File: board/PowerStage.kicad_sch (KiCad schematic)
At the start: 36 parts

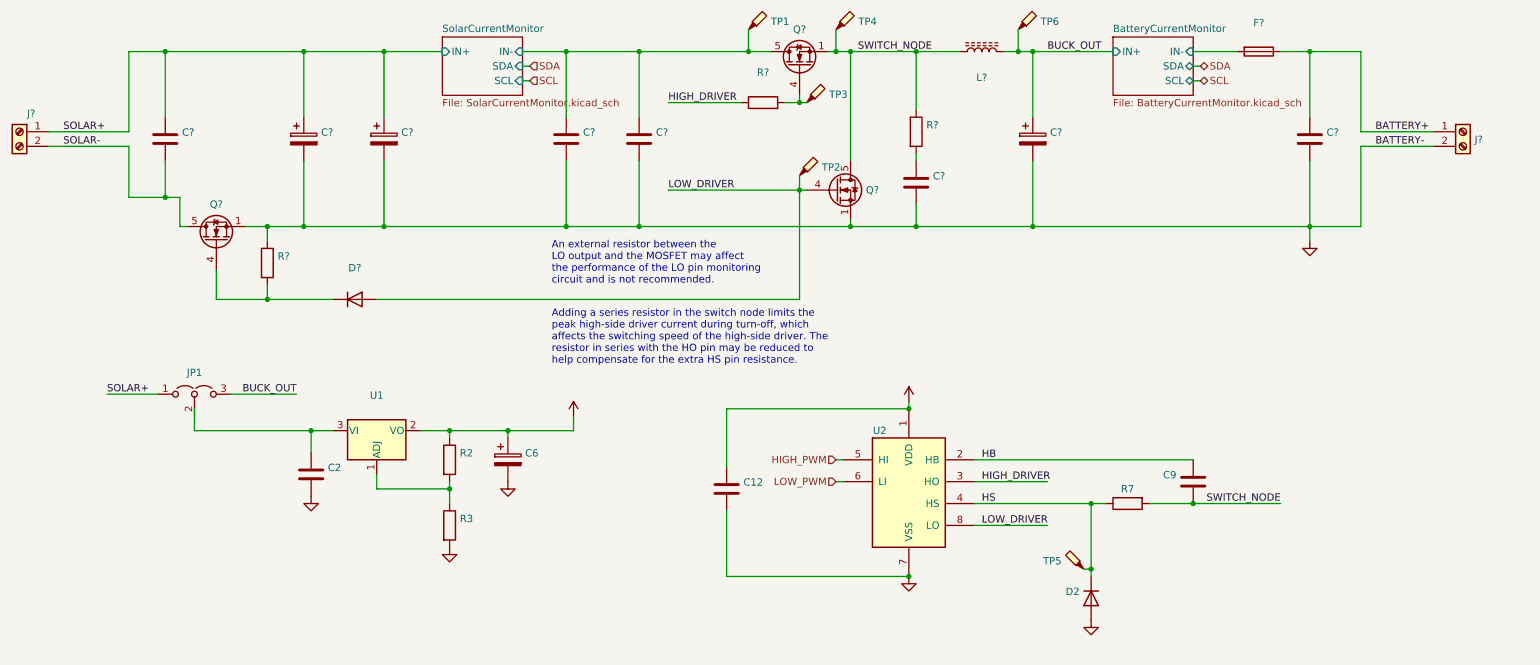
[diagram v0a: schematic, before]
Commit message: Different board layout, WIP
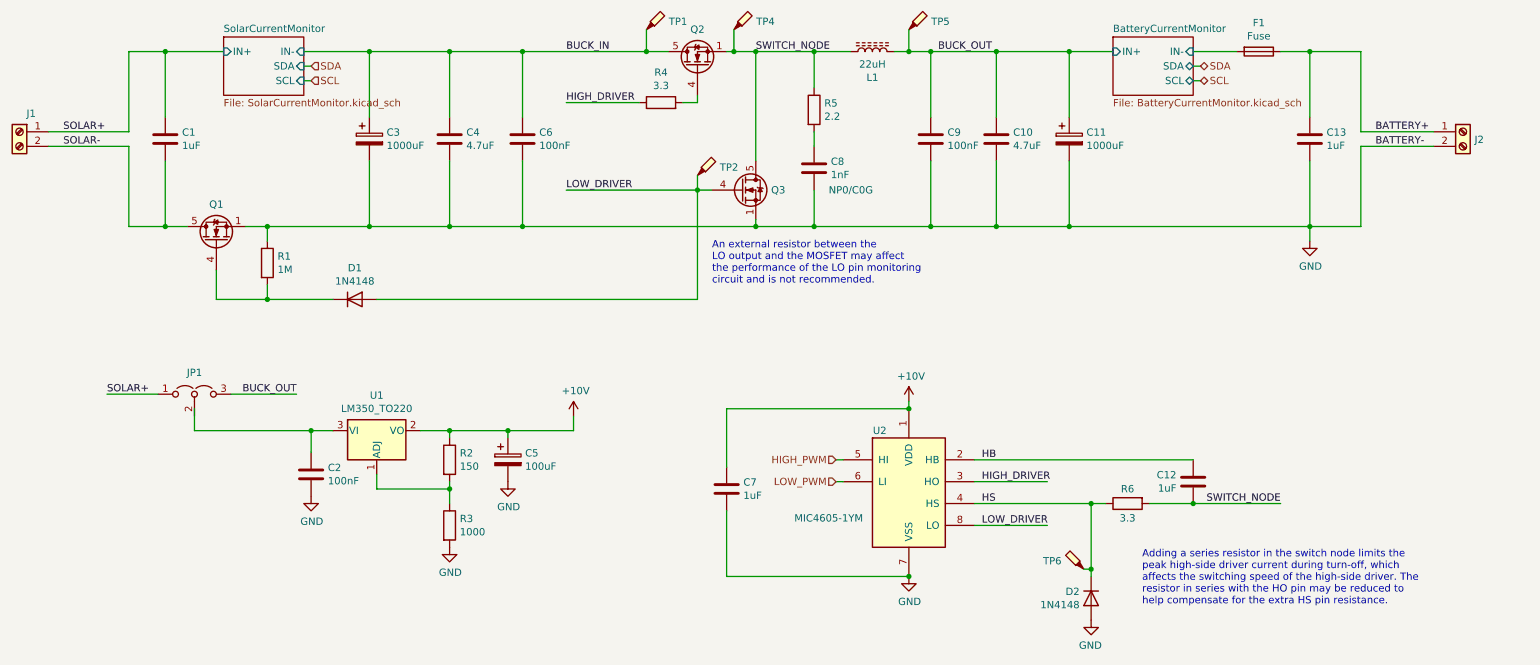
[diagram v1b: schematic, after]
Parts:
- removed C? (x2): (no value), symbol Device:C_Polarized
- removed C?: (no value), symbol Device:C
- removed TP3: (no value), symbol Connector:TestPoint_Probe
- added C10: 4.7uF, Capacitor_SMD:C_1210_3225Metric_Pad1.33x2.70mm_HandSolder, symbol Device:C
- added C11: 1000uF, SaintGimp:CP_16x25mm_horiz-L, symbol Device:C_Polarized
- added C6, C9: 100nF, Capacitor_SMD:C_0805_2012Metric_Pad1.18x1.45mm_HandSolder, symbol Device:C
- C1, C13: renamed from C?; value (none) -> 1uF; footprint (none) -> Capacitor_SMD:C_0805_2012Metric_Pad1.18x1.45mm_HandSolder
- C12: renamed from C9; value (none) -> 1uF; footprint (none) -> Capacitor_SMD:C_0805_2012Metric_Pad1.18x1.45mm_HandSolder
- C2: value (none) -> 100nF; footprint (none) -> Capacitor_SMD:C_0805_2012Metric_Pad1.18x1.45mm_HandSolder
- C3: renamed from C?; value (none) -> 1000uF; footprint (none) -> SaintGimp:CP_16x25mm_horiz-R
- C4: renamed from C?; value (none) -> 4.7uF; footprint (none) -> Capacitor_SMD:C_1210_3225Metric_Pad1.33x2.70mm_HandSolder
- C5: renamed from C6; value (none) -> 100uF; footprint (none) -> Capacitor_THT:CP_Radial_D6.3mm_P2.50mm
- C7: renamed from C12; value (none) -> 1uF; footprint (none) -> Capacitor_SMD:C_0805_2012Metric_Pad1.18x1.45mm_HandSolder
- C8: renamed from C?; value (none) -> 1nF; footprint (none) -> Capacitor_SMD:C_0805_2012Metric_Pad1.18x1.45mm_HandSolder; Remarks (none) -> NP0/C0G
- D1: renamed from D?; value (none) -> 1N4148; footprint (none) -> Diode_SMD:D_SOD-323_HandSoldering
- D2: value (none) -> 1N4148; footprint (none) -> Diode_SMD:D_SOD-323_HandSoldering
- F1: renamed from F?; value (none) -> Fuse; footprint (none) -> Fuse:Fuseholder_Blade_ATO_Littelfuse_Pudenz_2_Pin
- J1, J2: renamed from J?; value (none) -> Screw_Terminal_01x02; footprint (none) -> SaintGimp:Phoenix_Contact_MKDS_5-2-952
- JP1: value (none) -> Jumper_NC_Dual; footprint (none) -> Connector_PinHeader_2.54mm:PinHeader_1x03_P2.54mm_Vertical
- L1: renamed from L?; value (none) -> 22uH; footprint (none) -> SaintGimp:Coilcraft_SER2900
- Q1, Q2, Q3: renamed from Q?; value (none) -> PSMN5R5-60YS; footprint (none) -> Package_TO_SOT_SMD:LFPAK56
- R1: renamed from R?; value (none) -> 1M; footprint (none) -> Resistor_SMD:R_0805_2012Metric_Pad1.20x1.40mm_HandSolder
- R2: value (none) -> 150; footprint (none) -> Resistor_SMD:R_0805_2012Metric_Pad1.20x1.40mm_HandSolder
- R3: value (none) -> 1000; footprint (none) -> Resistor_SMD:R_0805_2012Metric_Pad1.20x1.40mm_HandSolder
- R4: renamed from R?; value (none) -> 3.3; footprint (none) -> Resistor_SMD:R_0805_2012Metric_Pad1.20x1.40mm_HandSolder
- R5: renamed from R?; value (none) -> 2.2; footprint (none) -> Resistor_SMD:R_1206_3216Metric_Pad1.30x1.75mm_HandSolder
- R6: renamed from R7; value (none) -> 3.3; footprint (none) -> Resistor_SMD:R_0805_2012Metric_Pad1.20x1.40mm_HandSolder
- TP1, TP2, TP4: value (none) -> TestPoint_Probe; footprint (none) -> TestPoint:TestPoint_Loop_D2.50mm_Drill1.0mm
- TP5: renamed from TP6; value (none) -> TestPoint_Probe; footprint (none) -> TestPoint:TestPoint_Loop_D2.50mm_Drill1.0mm
- TP6: renamed from TP5; value (none) -> TestPoint_Probe; footprint (none) -> TestPoint:TestPoint_Loop_D2.50mm_Drill1.0mm
- U1: value (none) -> LM350_TO220; footprint (none) -> Package_TO_SOT_THT:TO-220-3_Vertical
- U2: value (none) -> MIC4605-1YM; footprint (none) -> Package_SO:SOIC-8_3.9x4.9mm_P1.27mm
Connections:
- net BUCK_OUT: now also C10.1, C11.1, C9.1
- net GND: now also C10.2, C11.2, C6.2, C9.2
- net SOLAR+: no longer C3.1
- net SolarCurrentMonitor/IN- renamed BUCK_IN
- net BUCK_IN: now also C3.1, C6.1
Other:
- moved on the sheet: C3, C4, C8, L1, Q2, Q3, R4, R5, TP1, TP2, TP4, TP5
